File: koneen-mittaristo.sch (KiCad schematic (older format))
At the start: 16 parts, among them J2 J2 - Mittareiden sähkönsyöttö, J3 J3 - Maa, J4 J4 - Moottorin johtosarjan ky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

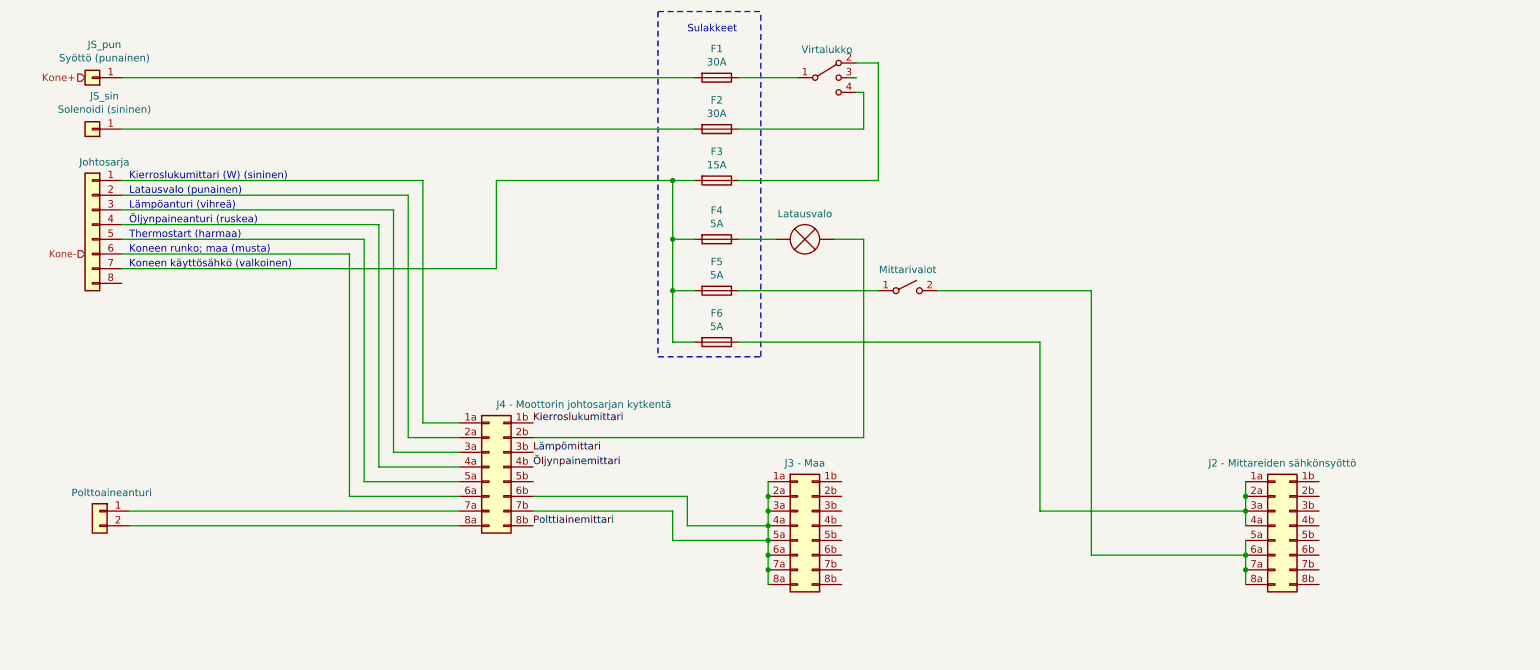
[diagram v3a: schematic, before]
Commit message: Kaapelien merkinnät toteutuneen johdotuksen mukaan
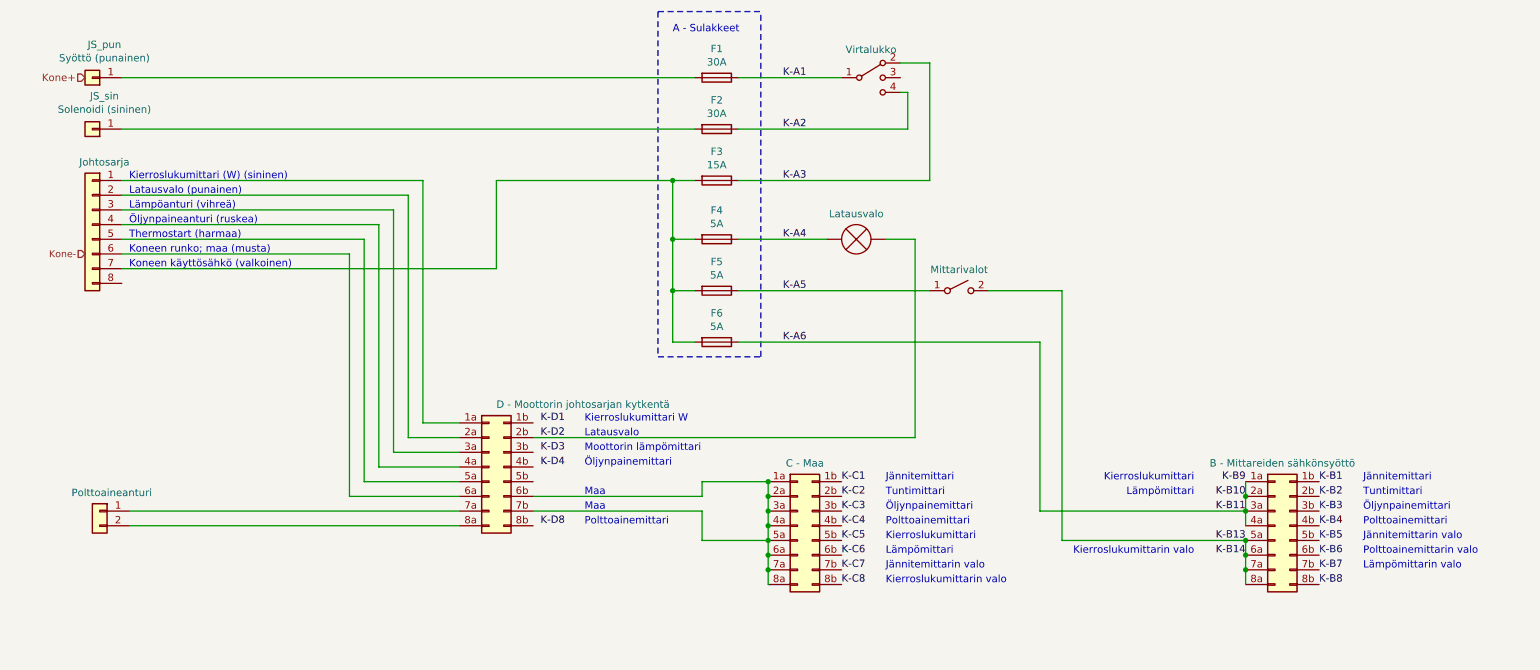
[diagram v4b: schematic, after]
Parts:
- J2: value J2 - Mittareiden sähkönsyöttö -> B - Mittareiden sähkönsyöttö
- J3: value J3 - Maa -> C - Maa
- J4: value J4 - Moottorin johtosarjan kytkentä -> D - Moottorin johtosarjan kytkentä
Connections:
- net K-A6: now reaches F6.1, J2.1a (Pin_1a), J2.2a (Pin_2a), J2.3a (Pin_3a), J2.4a (Pin_4a)
- net K-B1: now reaches J2.1b (Pin_1b)
- net K-B2: now reaches J2.2b (Pin_2b)
- net K-B3: now reaches J2.3b (Pin_3b)
- net K-B4: now reaches J2.4b (Pin_4b)
- net K-B13: now reaches J2.5a (Pin_5a), J2.6a (Pin_6a), J2.7a (Pin_7a), J2.8a (Pin_8a), Mittarivalot.2 (B)
- net K-B5: now reaches J2.5b (Pin_5b)
- net K-B6: now reaches J2.6b (Pin_6b)
- net K-B7: now reaches J2.7b (Pin_7b)
- net K-B8: now reaches J2.8b (Pin_8b)
- net K-D2: now reaches J4.2b (Pin_2b), Latausvalo.2 (+)
- net K-A5: now reaches F5.1, Mittarivalot.1 (A)
- net K-A1: now reaches F1.1, Virtalukko.1
- net K-A3: now reaches F3.1, Virtalukko.2
- net K-A2: now reaches F2.1, Virtalukko.4
- net K-A4: now reaches F4.1, Latausvalo.1 (-)
- net K-C1: now reaches J3.1b (Pin_1b)
- net K-C2: now reaches J3.2b (Pin_2b)
- net K-C3: now reaches J3.3b (Pin_3b)
- net K-C4: now reaches J3.4b (Pin_4b)
- net K-C5: now reaches J3.5b (Pin_5b)
- net K-C6: now reaches J3.6b (Pin_6b)
- net K-C7: now reaches J3.7b (Pin_7b)
- net K-C8: now reaches J3.8b (Pin_8b)
- net Kierroslukumittari: no longer names the net of J4.1b (Pin_1b)
- net Lämpömittari: no longer names the net of J4.3b (Pin_3b)
- net Polttiainemittari: no longer names the net of J4.8b (Pin_8b)
- net Öljynpainemittari: no longer names the net of J4.4b (Pin_4b)
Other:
- note added: "A - Sulakkeet"
- note added: "Jännitemittari"
- note added: "Jännitemittarin valo"
- note added: "Kierroslukumittari"
- note added: "Kierroslukumittari W"
- note added: "Kierroslukumittarin valo"
- note added: "Latausvalo"
- note added: "Lämpömittari"
- note added: "Lämpömittarin valo"
- note added: "Maa"
- note added: "Moottorin lämpömittari"
- note added: "Polttoainemittari"
- note added: "Polttoainemittarin valo"
- note added: "Tuntimittari"
- note added: "Öljynpainemittari"
- note removed: "Sulakkeet"
- moved on the sheet: Latausvalo, Mittarivalot, Virtalukko
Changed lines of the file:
@@
 Sheet 4 4
 Title "Särkänlinnan moottorin mittariston kytkentä"
-Date "2020-05-08-Draft"
+Date "2020-05-13-Draft"
 Rev "0"
 Comp "Merenkävijät ry"
@@
 P 9350 4100
 F 0 "J2" H 9400 4525 50  0001 C CNN
-F 1 "J2 - Mittareiden sähkönsyöttö" H 9400 4526 50  0000 C CNN
+F 1 "B - Mittareiden sähkönsyöttö" H 9400 4526 50  0000 C CNN
 F 2 "" H 9350 4100 50  0001 C CNN
 F 3 "~" H 9350 4100 50  0001 C CNN
@@
 P 4000 3700
 F 0 "J4" H 4050 4125 50  0001 C CNN
-F 1 "J4 - Moottorin johtosarjan kytkentä" H 4050 4126 50  0000 L CNN
+F 1 "D - Moottorin johtosarjan kytkentä" H 4050 4126 50  0000 L CNN
 F 2 "" H 4000 3700 50  0001 C CNN
 F 3 "~" H 4000 3700 50  0001 C CNN
@@
 L Switch:SW_SPST Mittarivalot
 U 1 1 5DE1A355
-P 6850 2500
-F 0 "Mittarivalot" H 6850 2643 50  0000 C CNN
-F 1 "SW_SPST" H 6850 2644 50  0001 C CNN
-F 2 "" H 6850 2500 50  0001 C CNN
-F 3 "~" H 6850 2500 50  0001 C CNN
-	1    6850 2500
+P 7200 2500
+F 0 "Mittarivalot" H 7200 2643 50  0000 C CNN
+F 1 "SW_SPST" H 7200 2644 50  0001 C CNN
+F 2 "" H 7200 2500 50  0001 C CNN
+F 3 "~" H 7200 2500 50  0001 C CNN
+	1    7200 2500
 	1    0    0    -1
 $EndComp
@@
 L SL-sahkot-rescue:SL-virtalukko-Switch Virtalukko
 U 1 1 5DE340D4
-P 6300 1050
-F 0 "Virtalukko" H 6300 1241 50  0000 C CNN
-F 1 "SL-virtalukko" H 6300 1242 50  0001 C CNN
-F 2 "" H 5675 1225 50  0001 C CNN
-F 3 "~" H 5675 1225 50  0001 C CNN
-	1    6300 1050
+P 6600 1050
+F 0 "Virtalukko" H 6600 1241 50  0000 C CNN
+F 1 "SL-virtalukko" H 6600 1242 50  0001 C CNN
+F 2 "" H 5975 1225 50  0001 C CNN
+F 3 "~" H 5975 1225 50  0001 C CNN
+	1    6600 1050
 	1    0    0    -1
 $EndComp
@@
 L Device:Lamp Latausvalo
 U 1 1 5DE611EB
-P 6150 2150
-F 0 "Latausvalo" V 5977 2150 50  0000 C CNN
-F 1 "Lamp" H 6278 2105 50  0001 L CNN
-F 2 "" V 6150 2250 50  0001 C CNN
-F 3 "~" V 6150 2250 50  0001 C CNN
-	1    6150 2150
+P 6500 2150
+F 0 "Latausvalo" V 6327 2150 50  0000 C CNN
+F 1 "Lamp" H 6628 2105 50  0001 L CNN
+F 2 "" V 6500 2250 50  0001 C CNN
+F 3 "~" V 6500 2250 50  0001 C CNN
+	1    6500 2150
 	0    1    1    0
 $EndComp
@@
 	5250 2150 5250 2500
 Wire Wire Line
-	6500 1150 6550 1150
-Wire Wire Line
-	6650 950  6500 950
-Wire Wire Line
-	6450 1050 6500 1050
+	6800 1150 6850 1150
+Wire Wire Line
+	7000 950  6800 950
 Text Notes 1550 1750 0    50   ~ 0
 Kierroslukumittari (W) (sininen)
@@
 Wire Notes Line
 	5150 600  5850 600
-Text Notes 5350 750  0    50   ~ 0
-Sulakkeet
-Wire Wire Line
-	4300 3500 6550 3500
-Wire Wire Line
-	5700 2150 5950 2150
+Text Notes 5250 750  0    50   ~ 0
+A - Sulakkeet
 Wire Wire Line
 	5400 1050 1500 1050
 Wire Wire Line
-	5700 1050 6100 1050
+	5700 1050 6400 1050
 $Comp
 L Connector_Generic:Conn_02x08_Row_Letter_Last J3
@@
 P 6100 4100
 F 0 "J3" H 6150 4525 50  0001 C CNN
-F 1 "J3 - Maa" H 6150 4526 50  0000 C CNN
+F 1 "C - Maa" H 6150 4526 50  0000 C CNN
 F 2 "" H 6100 4100 50  0001 C CNN
 F 3 "~" H 6100 4100 50  0001 C CNN
@@
 	3450 1850 3450 3500
 Wire Wire Line
-	6550 1150 6550 1400
-Wire Wire Line
-	6550 1400 5700 1400
+	6850 1150 6850 1400
+Wire Wire Line
+	6850 1400 5700 1400
 Wire Wire Line
 	1500 1400 5400 1400
 Wire Wire Line
-	6650 950  6650 1750
-Wire Wire Line
-	5700 1750 6650 1750
+	7000 950  7000 1750
+Wire Wire Line
+	5700 1750 7000 1750
 Wire Wire Line
 	5250 1750 4050 1750
@@
 	3050 3900 3800 3900
 Wire Wire Line
-	5350 4100 5900 4100
-Wire Wire Line
-	5350 4100 5350 3900
-Wire Wire Line
-	5350 3900 4300 3900
-Wire Wire Line
-	4300 4000 5250 4000
-Wire Wire Line
-	5250 4000 5250 4200
-Wire Wire Line
-	5250 4200 5900 4200
+	5450 3900 4300 3900
+Wire Wire Line
+	4300 4000 5450 4000
+Wire Wire Line
+	5450 4000 5450 4200
+Wire Wire Line
+	5450 4200 5900 4200
 Wire Wire Line
 	5250 2500 5400 2500
@@
 Connection ~ 5250 2500
 Wire Wire Line
-	6550 2150 6550 3500
-Wire Wire Line
-	6550 2150 6350 2150
-Wire Wire Line
-	5700 2500 6650 2500
+	6900 2150 6900 3500
+Wire Wire Line
+	6900 2150 6700 2150
 Connection ~ 9150 4300
 Wire Wire Line
@@
 Connection ~ 9150 4000
 Wire Wire Line
-	8100 4300 9150 4300
-Wire Wire Line
-	8100 2500 8100 4300
-Wire Wire Line
 	9150 4000 7750 4000
 Wire Wire Line
@@
 Wire Wire Line
 	3150 2150 1500 2150
-Text Label 4300 3400 0    50   ~ 0
+Wire Wire Line
+	7400 2500 7900 2500
+Wire Wire Line
+	4300 3500 6900 3500
+Wire Wire Line
+	5700 2150 6300 2150
+Wire Wire Line
+	5700 2500 7000 2500
+Text Label 6000 1050 0    50   ~ 0
+K-A1
+Text Label 6000 1400 0    50   ~ 0
+K-A2
+Text Label 6000 1750 0    50   ~ 0
+K-A3
+Text Label 6000 2150 0    50   ~ 0
+K-A4
+Text Label 6000 2500 0    50   ~ 0
+K-A5
+Text Label 6000 2850 0    50   ~ 0
+K-A6
+Text Label 4350 3400 0    50   ~ 0
+K-D1
+Text Label 4350 3500 0    50   ~ 0
+K-D2
+Text Label 4350 3600 0    50   ~ 0
+K-D3
+Text Label 4350 3700 0    50   ~ 0
+K-D4
+Text Label 4350 4100 0    50   ~ 0
+K-D8
+Text Notes 4650 3400 0    50   ~ 0
+Kierroslukumittari W
+Text Notes 4650 3500 0    50   ~ 0
+Latausvalo
+Text Notes 4650 3600 0    50   ~ 0
+Moottorin lämpömittari
+Text Notes 4650 3700 0    50   ~ 0
+Öljynpainemittari
+Text Notes 4650 4100 0    50   ~ 0
+Polttoainemittari
+Wire Wire Line
+	5450 3900 5450 3800
+Wire Wire Line
+	5450 3800 5900 3800
+Connection ~ 5900 3800
+Text Notes 4650 3900 0    50   ~ 0
+Maa
+Text Notes 4650 4000 0    50   ~ 0
+Maa
+Text Label 6400 3800 0    50   ~ 0
+K-C1
+Text Label 6400 3900 0    50   ~ 0
+K-C2
+Text Label 6400 4000 0    50   ~ 0
+K-C3
+Text Label 6400 4100 0    50   ~ 0
+K-C4
+Text Label 6400 4200 0    50   ~ 0
+K-C5
+Text Label 6400 4300 0    50   ~ 0
+K-C6
+Text Label 6400 4400 0    50   ~ 0
+K-C7
+Text Label 6400 4500 0    50   ~ 0
+K-C8
+Text Label 9650 3800 0    50   ~ 0
+K-B1
+Text Label 9650 3900 0    50   ~ 0
+K-B2
+Text Label 9650 4000 0    50   ~ 0
+K-B3
+Text Label 9650 4100 0    50   ~ 0
+K-B4
+Text Label 9650 4200 0    50   ~ 0
+K-B5
+Text Label 9650 4300 0    50   ~ 0
+K-B6
+Text Label 9650 4400 0    50   ~ 0
+K-B7
+Text Label 9650 4500 0    50   ~ 0
+K-B8
+Text Label 9150 3800 2    50   ~ 0
+K-B9
+Text Label 9150 3900 2    50   ~ 0
+K-B10
+Wire Wire Line
+	9150 4200 7900 4200
+Wire Wire Line
+	7900 2500 7900 4200
+Connection ~ 9150 4200
+Text Label 9150 4300 2    50   ~ 0
+K-B14
+Text Notes 6700 3800 0    50   ~ 0
+Jännitemittari
+Text Notes 6700 3900 0    50   ~ 0
+Tuntimittari
+Text Notes 6700 4000 0    50   ~ 0
+Öljynpainemittari
+Text Notes 6700 4100 0    50   ~ 0
+Polttoainemittari
+Text Notes 6700 4200 0    50   ~ 0
 Kierroslukumittari
-Text Label 4300 3600 0    50   ~ 0
+Text Notes 6700 4300 0    50   ~ 0
 Lämpömittari
-Text Label 4300 3700 0    50   ~ 0
+Text Notes 6700 4400 0    50   ~ 0
+Jännitemittarin valo
+Text Notes 6700 4500 0    50   ~ 0
+Kierroslukumittarin valo
+Text Notes 9950 3800 0    50   ~ 0
+Jännitemittari
+Text Notes 9950 3900 0    50   ~ 0
+Tuntimittari
+Text Notes 9950 4000 0    50   ~ 0
 Öljynpainemittari
-Text Label 4300 4100 0    50   ~ 0
-Polttiainemittari
-Wire Wire Line
-	7050 2500 8100 2500
+Text Notes 9950 4100 0    50   ~ 0
+Polttoainemittari
+Text Notes 9950 4200 0    50   ~ 0
+Jännitemittarin valo
+Text Notes 9950 4300 0    50   ~ 0
+Polttoainemittarin valo
+Text Notes 9950 4400 0    50   ~ 0
+Lämpömittarin valo
+Text Notes 8800 3800 2    50   ~ 0
+Kierroslukumittari
+Text Notes 8800 3900 2    50   ~ 0
+Lämpömittari
+Text Notes 8800 4300 2    50   ~ 0
+Kierroslukumittarin valo
+Text Label 9150 4000 2    50   ~ 0
+K-B11
+Text Label 9150 4200 2    50   ~ 0
+K-B13
 $EndSCHEMATC

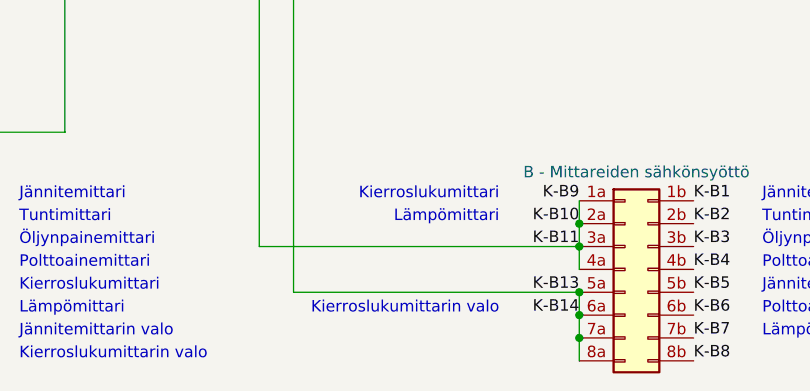
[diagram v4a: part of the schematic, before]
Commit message: Add label for mitterivalokytkin into the engine schematic
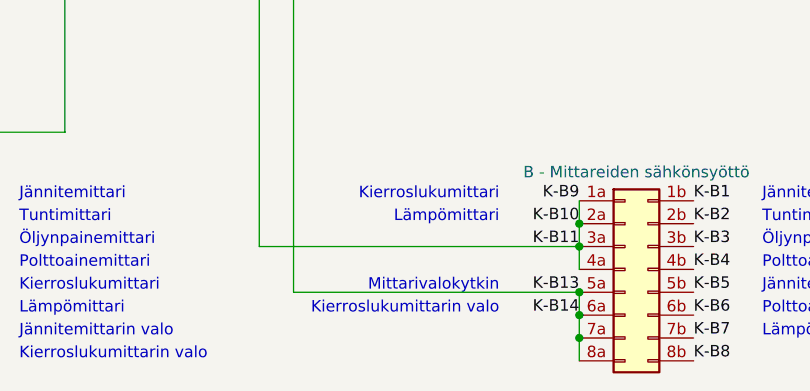
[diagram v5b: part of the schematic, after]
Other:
- note added: "Mittarivalokytkin"
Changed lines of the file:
@@
 Sheet 4 4
 Title "Särkänlinnan moottorin mittariston kytkentä"
-Date "2020-05-13-Draft"
+Date "2020-05-21"
 Rev "0"
-Comp "Merenkävijät ry"
+Comp "Merenkävijät ry (JA)"
 Comment1 ""
 Comment2 ""
@@
 Text Label 9150 4200 2    50   ~ 0
 K-B13
+Text Notes 8800 4200 2    50   ~ 0
+Mittarivalokytkin
 $EndSCHEMATC
